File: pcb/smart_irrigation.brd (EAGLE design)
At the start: 100 x 80 mm, 24 parts, among them IC1 7805DT, IC2 7833DT, IC3 TMP36, J1 1X2-3.5MM, Q2 32.768

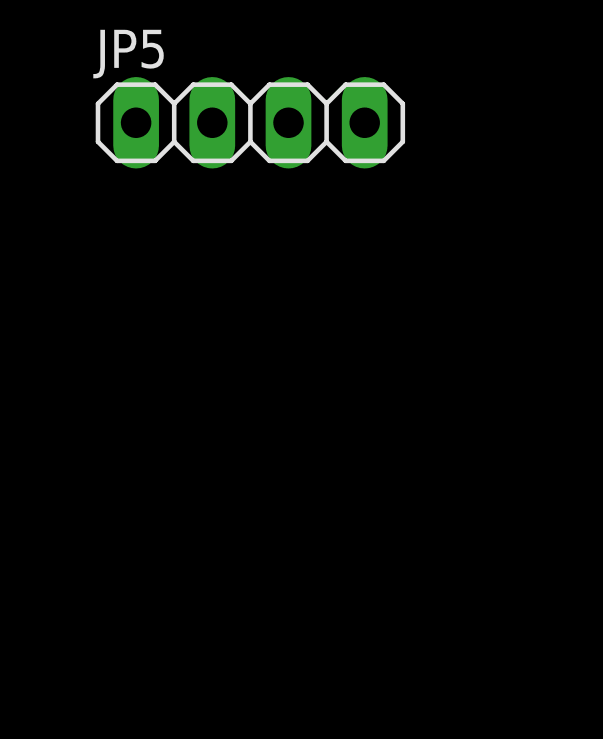
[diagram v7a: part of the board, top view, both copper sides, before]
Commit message: PCB: Add caps across BL600 power input
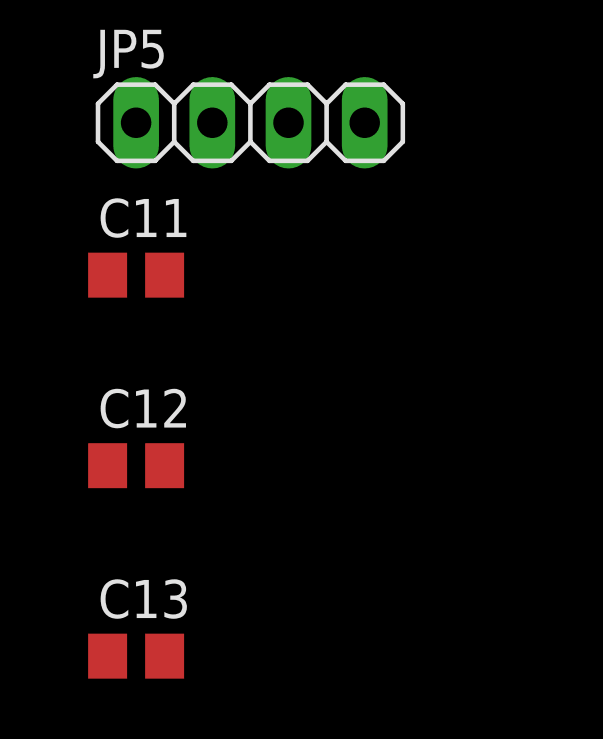
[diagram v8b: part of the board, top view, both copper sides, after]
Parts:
- added C11, C12, C13: 10uF, rcl:C0805
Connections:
- net +3V3: now also C11.1, C12.1, C13.1
- net GND: now also C11.2, C12.2, C13.2
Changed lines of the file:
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@@
 <element name="JP4" library="pinhead" package="1X03" value="" x="-71.12" y="-144.78"/>
 <element name="JP5" library="smart_irrigation" package="1X04" value="" x="-69.85" y="-151.13"/>
+<element name="C11" library="rcl" package="C0805" value="10uF" x="-73.66" y="-156.21"/>
+<element name="C12" library="rcl" package="C0805" value="10uF" x="-73.66" y="-162.56"/>
+<element name="C13" library="rcl" package="C0805" value="10uF" x="-73.66" y="-168.91"/>
 </elements>
 <signals>
@@
 <contactref element="C9" pad="2"/>
 <contactref element="C10" pad="2"/>
-<contactref element="JP1" pad="1"/>
-<contactref element="JP1" pad="4"/>
-<contactref element="U$1" pad="J5_1"/>
-<contactref element="U$1" pad="J5_4"/>
 <contactref element="JP3" pad="16"/>
 <contactref element="U$1" pad="11"/>
@@
 <contactref element="U$1" pad="28"/>
 <contactref element="JP3" pad="1"/>
+<contactref element="C11" pad="2"/>
+<contactref element="C13" pad="2"/>
+<contactref element="C12" pad="2"/>
+<contactref element="JP1" pad="4"/>
+<contactref element="U$1" pad="J5_4"/>
+<contactref element="JP1" pad="1"/>
+<contactref element="U$1" pad="J5_1"/>
+<wire x1="-72.71" y1="-162.56" x2="-72.71" y2="-168.91" width="0" layer="19" extent="1-1"/>
+<wire x1="-72.71" y1="-156.21" x2="-72.71" y2="-162.56" width="0" layer="19" extent="1-1"/>
+<wire x1="-71.12" y1="-151.13" x2="-72.71" y2="-156.21" width="0" layer="19" extent="1-1"/>
 <wire x1="-71.12" y1="-144.78" x2="-71.12" y2="-151.13" width="0" layer="19" extent="1-1"/>
 <wire x1="-71.12" y1="-138.43" x2="-71.12" y2="-144.78" width="0" layer="19" extent="1-1"/>
@@
 <contactref element="C3" pad="1"/>
 <contactref element="C10" pad="1"/>
-<contactref element="JP1" pad="3"/>
-<contactref element="JP1" pad="6"/>
-<contactref element="U$1" pad="J5_3"/>
-<contactref element="U$1" pad="J5_6"/>
 <contactref element="R2" pad="2"/>
 <contactref element="R1" pad="2"/>
@@
 <contactref element="JP4" pad="1"/>
 <contactref element="JP5" pad="1"/>
+<contactref element="C11" pad="1"/>
+<contactref element="C13" pad="1"/>
+<contactref element="C12" pad="1"/>
+<contactref element="JP1" pad="6"/>
+<contactref element="U$1" pad="J5_6"/>
+<contactref element="JP1" pad="3"/>
+<contactref element="U$1" pad="J5_3"/>
+<wire x1="-74.61" y1="-162.56" x2="-74.61" y2="-168.91" width="0" layer="19" extent="1-1"/>
+<wire x1="-74.61" y1="-156.21" x2="-74.61" y2="-162.56" width="0" layer="19" extent="1-1"/>
+<wire x1="-73.66" y1="-151.13" x2="-74.61" y2="-156.21" width="0" layer="19" extent="1-1"/>
 <wire x1="-73.66" y1="-144.78" x2="-73.66" y2="-151.13" width="0" layer="19" extent="1-1"/>
 <wire x1="-73.66" y1="-138.43" x2="-73.66" y2="-144.78" width="0" layer="19" extent="1-1"/>
